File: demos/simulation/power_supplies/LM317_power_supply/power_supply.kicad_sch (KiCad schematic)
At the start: 14 parts, among them T1 Transformer_1P_1S, U1 LM317_TO-220

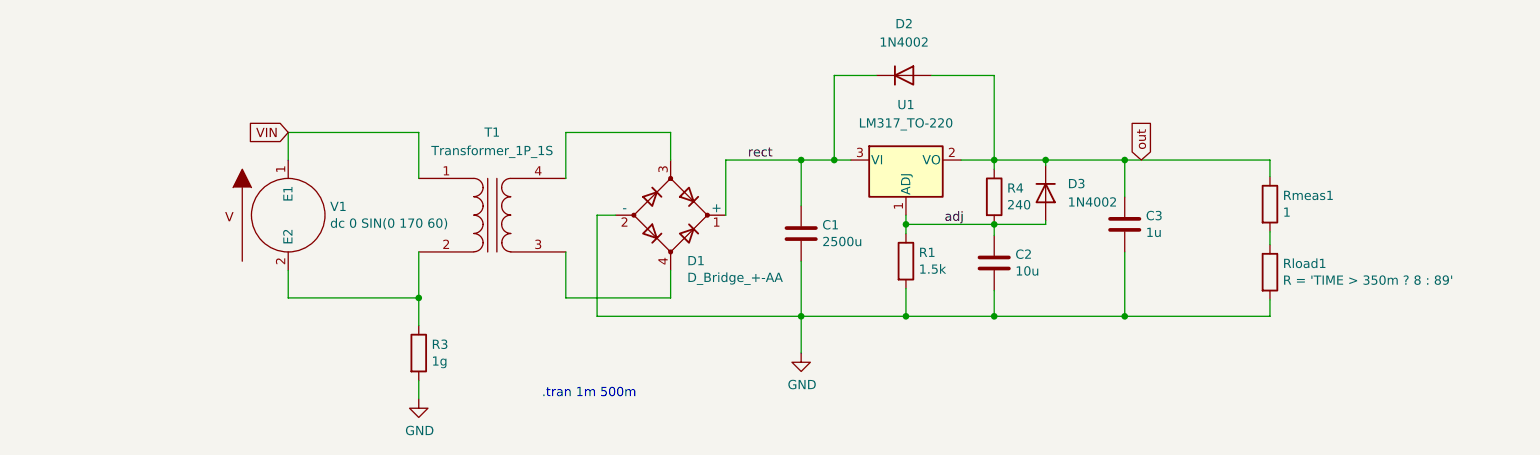
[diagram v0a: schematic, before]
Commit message: Update LM317 simulation example
Use modern symbols
Align to grid
Show interesting simulation parameters
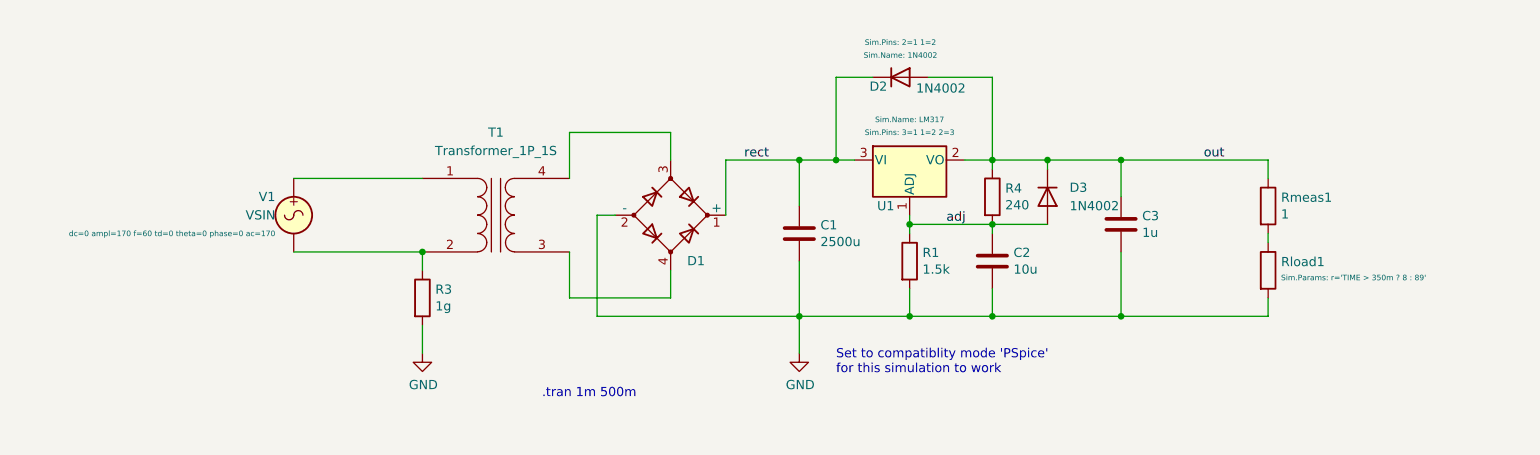
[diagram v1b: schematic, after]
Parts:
- removed V1: dc 0 SIN(0 170 60), symbol pspice:VSOURCE
- added V1: VSIN, symbol Simulation_SPICE:VSIN
- Rload1: value R = 'TIME > 350m ? 8 : 89' -> ~
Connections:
- net at R3.1, T1.2 (AB): now also V1.2
- net VIN: no longer names the net of T1.1 (AA)
- net VIN: now also V1.1
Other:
- note added: "Set to compatiblity mode 'PSpice' for this simulation to work"
- moved on the sheet: C3, D2, D3, R1, R3, T1, U1
